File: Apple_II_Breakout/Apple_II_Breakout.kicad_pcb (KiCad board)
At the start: 2 copper layers, 99.9 x 80 mm, 8 parts, among them J1 Conn_01x08_Male, J2 Conn_02x25_Counter_Clockwise, J3 Conn_01x08_Male, J4 Conn_02x25_Counter_Clockwise, J5 Conn_02x40_Top_Bottom, J6 Conn_02x40_Top_Bottom, J7 Conn_02x40_Top_Bottom

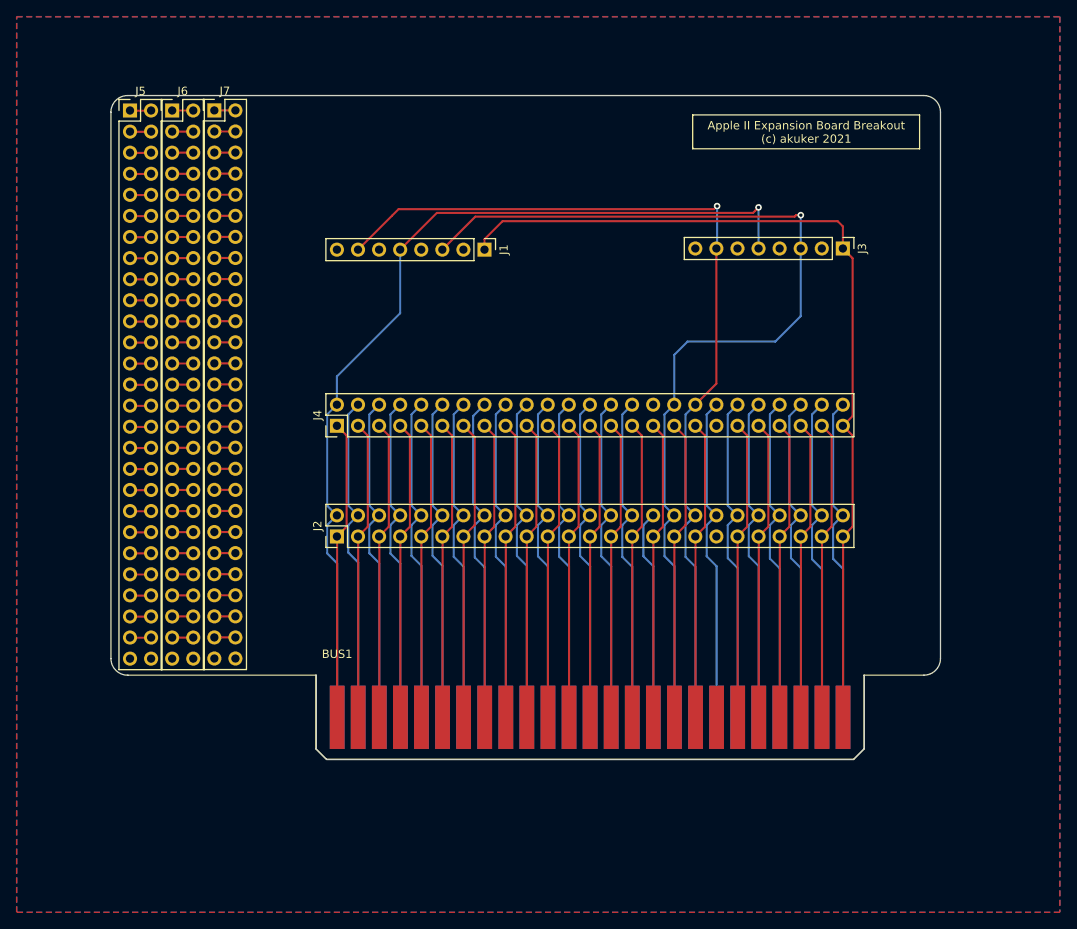
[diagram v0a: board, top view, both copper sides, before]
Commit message: Finished up Apple II breakout
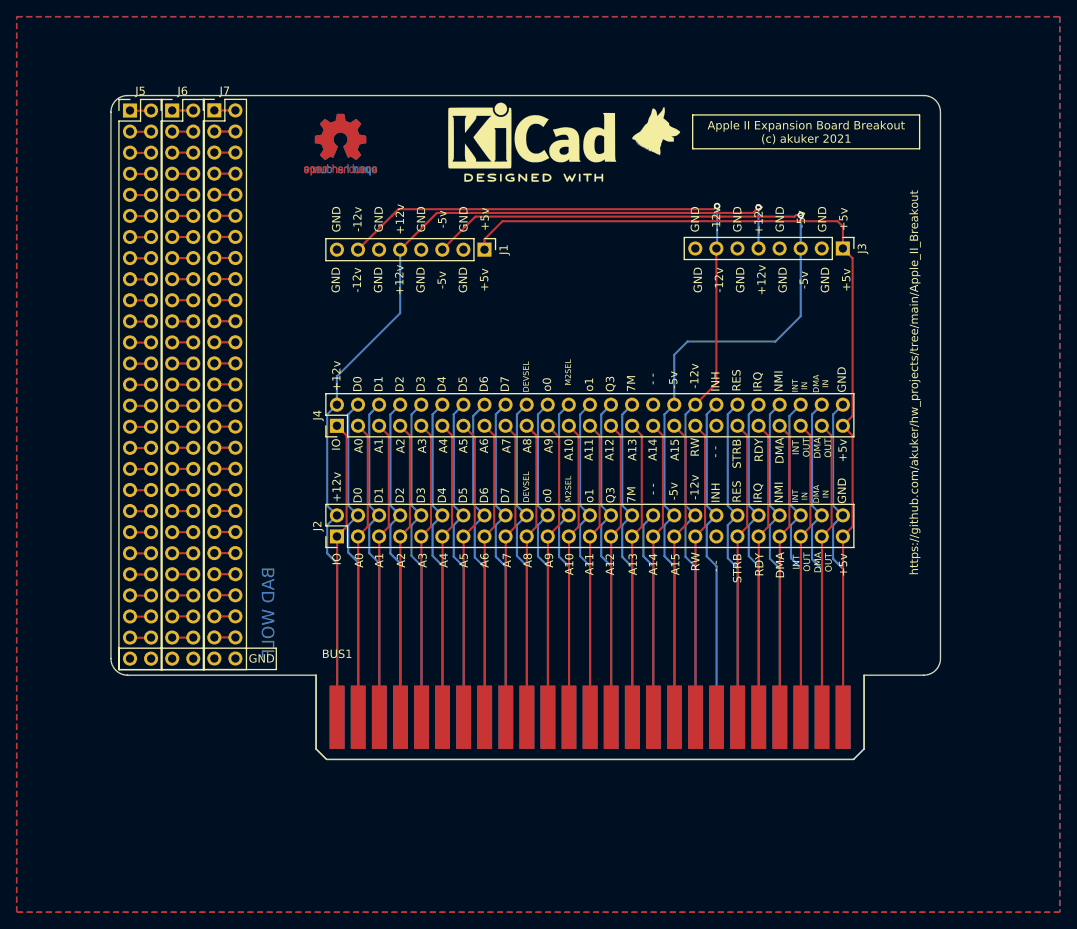
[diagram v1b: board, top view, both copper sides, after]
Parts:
- added G***: LOGO, Apple_II_Breakout:gsd, F.Cu at (172.9, 50.9)
- added REF**: KiCad-Logo2_8mm_SilkScreen, Symbol:KiCad-Logo2_8mm_SilkScreen, F.Cu at (158.0, 51.4)
- added REF**: OSHW-Logo2_9.8x8mm_Copper, Symbol:OSHW-Logo2_9.8x8mm_Copper, B.Cu at (134.9, 52.6)
- added REF**: OSHW-Logo2_9.8x8mm_Copper, Symbol:OSHW-Logo2_9.8x8mm_Copper, F.Cu at (134.9, 52.5)
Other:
- board text added: "+12v"
- board text added: "+5v"
- board text added: "- -"
- board text added: "-12v"
- board text added: "-5v"
- board text added: "7M"
- board text added: "A0"
- board text added: "A1"
- board text added: "A10"
- board text added: "A11"
- board text added: "A12"
- board text added: "A13"
- board text added: "A14"
- board text added: "A15"
- board text added: "A2"
- board text added: "A3"
- board text added: "A4"
- board text added: "A5"
- board text added: "A6"
- board text added: "A7"
- board text added: "A8"
- board text added: "A9"
- board text added: "BAD WOLF"
- board text added: "D0"
- board text added: "D1"
- board text added: "D2"
- board text added: "D3"
- board text added: "D4"
- board text added: "D5"
- board text added: "D6"
- board text added: "D7"
- board text added: "DEVSEL"
- board text added: "DMA"
- board text added: "DMA IN"
- board text added: "DMA OUT"
- board text added: "GND"
- board text added: "INH"
- board text added: "INT IN"
- board text added: "INT OUT"
- board text added: "IO"
- board text added: "IRQ"
- board text added: "M2SEL"
- board text added: "NMI"
- board text added: "Q3"
- board text added: "RDY"
- board text added: "RES"
- board text added: "RW"
- board text added: "STRB"
- board text added: "https://github.com/akuker/hw_projects/tree/main/Apple_II_Breakout"
- board text added: "o0"
- board text added: "o1"
